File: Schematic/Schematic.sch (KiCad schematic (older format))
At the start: 28 parts, among them M1 Motor_DC, M2 Motor_DC

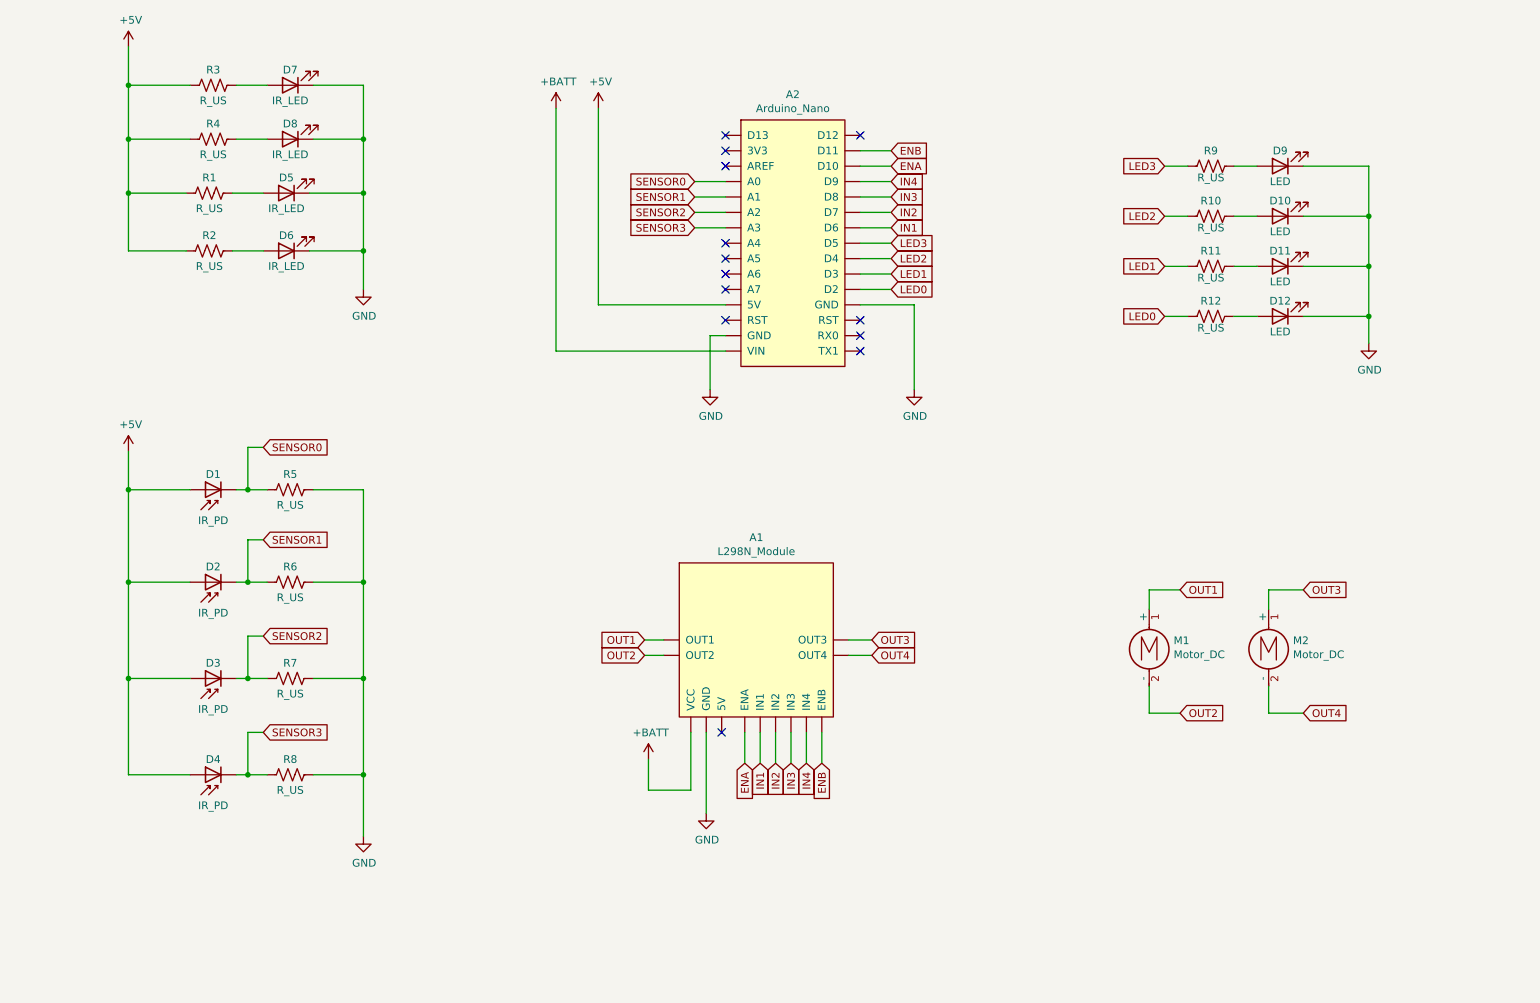
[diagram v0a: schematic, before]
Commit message: Update Schematic
- Rename Global Label
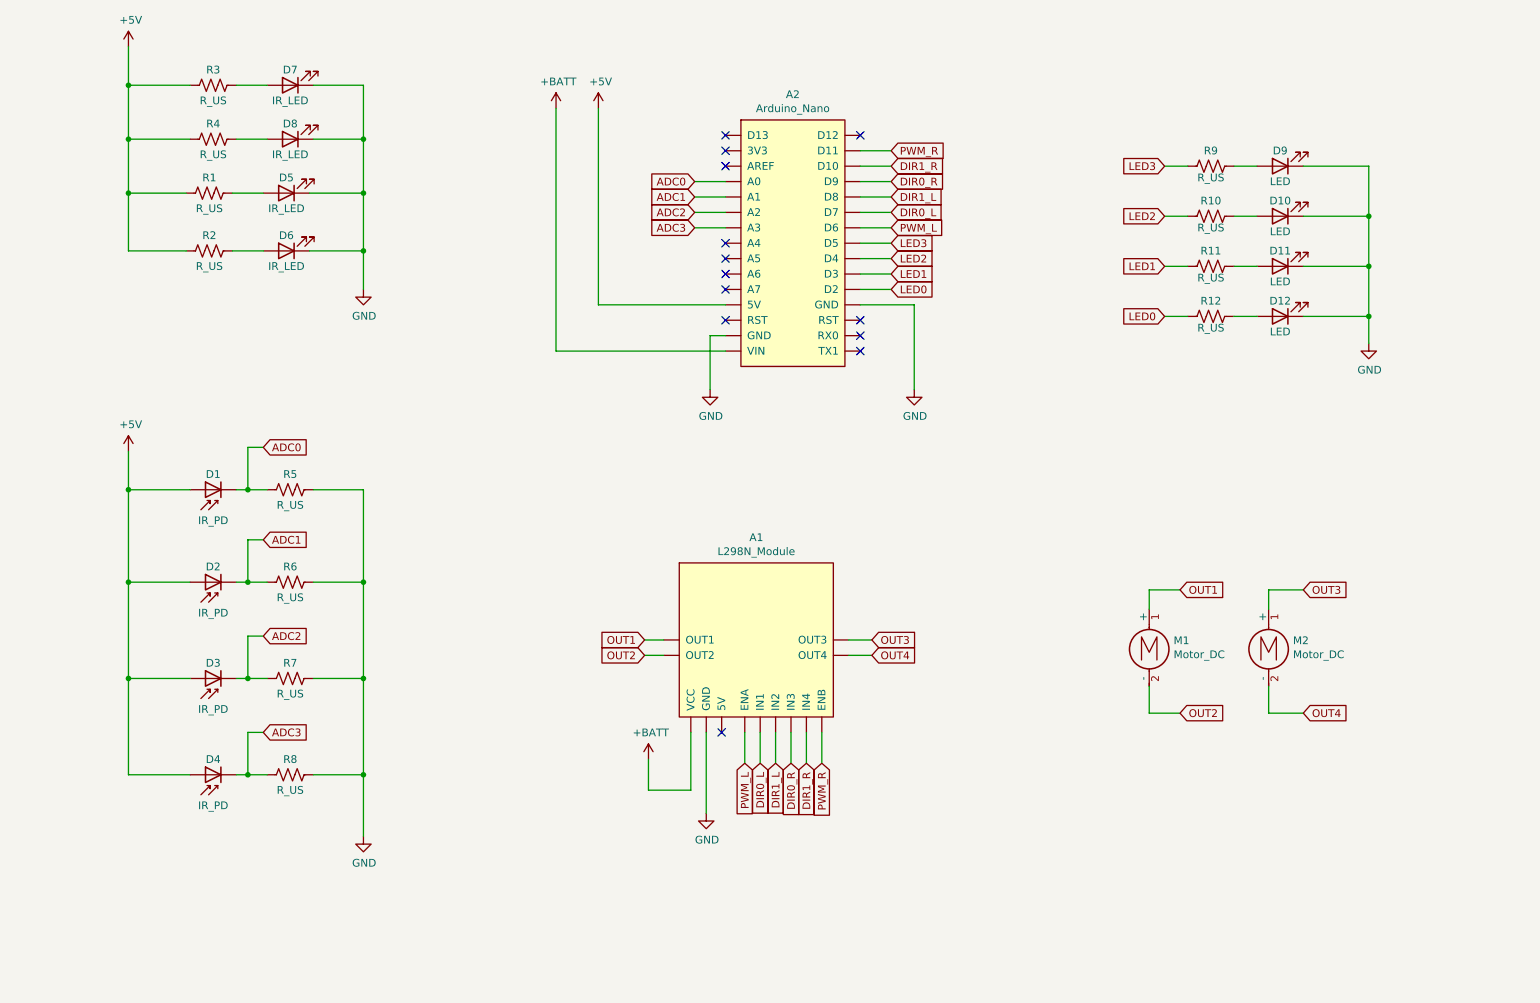
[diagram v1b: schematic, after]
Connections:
- net ENA is gone; now on net PWM_R: A1.~ (VCC), A2.~ (VIN)
- net ENB is gone; now on net PWM_R: A1.~ (VCC), A2.~ (VIN)
- net IN1 is gone; now on net PWM_R: A1.~ (VCC), A2.~ (VIN)
- net IN2 is gone; now on net PWM_R: A1.~ (VCC), A2.~ (VIN)
- net IN3 is gone; now on net PWM_R: A1.~ (VCC), A2.~ (VIN)
- net IN4 is gone; now on net PWM_R: A1.~ (VCC), A2.~ (VIN)
- net PWM_R: now reaches A2.~ (VIN)
- net SENSOR0 renamed ADC0
- net SENSOR1 renamed ADC1
- net SENSOR2 renamed ADC2
- net SENSOR3 renamed ADC3
- new net DIR0_L: A1.~ (VCC), A2.~ (VIN)
- new net DIR0_R: A1.~ (VCC), A2.~ (VIN)
- new net DIR1_L: A1.~ (VCC), A2.~ (VIN)
- new net DIR1_R: A1.~ (VCC), A2.~ (VIN)
- new net PWM_L: A1.~ (VCC), A2.~ (VIN)
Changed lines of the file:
@@
 $EndComp
 Text GLabel 5850 5775 3    50   Input ~ 0
-IN2
+DIR1_L
 Wire Wire Line
 	5850 5575 5850 5775
 Text GLabel 5750 5775 3    50   Input ~ 0
-IN1
+DIR0_L
 Wire Wire Line
 	5750 5575 5750 5775
 Text GLabel 5950 5775 3    50   Input ~ 0
-IN3
+DIR0_R
 Wire Wire Line
 	5950 5575 5950 5775
 Text GLabel 6050 5775 3    50   Input ~ 0
-IN4
+DIR1_R
 Wire Wire Line
 	6050 5575 6050 5775
-Text GLabel 6600 2200 2    50   Input ~ 0
-IN2
 Wire Wire Line
 	6400 2200 6600 2200
-Text GLabel 6600 2300 2    50   Input ~ 0
-IN1
 Wire Wire Line
 	6400 2300 6600 2300
-Text GLabel 6600 2100 2    50   Input ~ 0
-IN3
 Wire Wire Line
 	6400 2100 6600 2100
-Text GLabel 6600 2000 2    50   Input ~ 0
-IN4
 Wire Wire Line
 	6400 2000 6600 2000
-Text GLabel 5650 5775 3    50   Input ~ 0
-ENA
 Wire Wire Line
 	5650 5575 5650 5775
-Text GLabel 6150 5775 3    50   Input ~ 0
-ENB
 Wire Wire Line
 	6150 5575 6150 5775
-Text GLabel 6600 1900 2    50   Input ~ 0
-ENA
 Wire Wire Line
 	6400 1900 6600 1900
-Text GLabel 6600 1800 2    50   Input ~ 0
-ENB
 Wire Wire Line
 	6400 1800 6600 1800
@@
 	2850 4000 3175 4000
 Text GLabel 2525 3725 2    50   Input ~ 0
-SENSOR0
+ADC0
 Wire Wire Line
 	2525 3725 2425 3725
@@
 	2850 4600 3175 4600
 Text GLabel 2525 4325 2    50   Input ~ 0
-SENSOR1
+ADC1
 Wire Wire Line
 	2525 4325 2425 4325
@@
 	2850 5850 3175 5850
 Text GLabel 2525 5575 2    50   Input ~ 0
-SENSOR3
+ADC3
 Wire Wire Line
 	2525 5575 2425 5575
@@
 	2525 4950 2425 4950
 Text GLabel 2525 4950 2    50   Input ~ 0
-SENSOR2
+ADC2
 $Comp
 L power:GND #PWR04
@@
 $EndComp
 Text GLabel 5325 2000 0    50   Input ~ 0
-SENSOR0
+ADC0
 Wire Wire Line
 	5325 2000 5525 2000
 Text GLabel 5325 2100 0    50   Input ~ 0
-SENSOR1
+ADC1
 Wire Wire Line
 	5325 2100 5525 2100
 Text GLabel 5325 2200 0    50   Input ~ 0
-SENSOR2
+ADC2
 Wire Wire Line
 	5325 2200 5525 2200
 Text GLabel 5325 2300 0    50   Input ~ 0
-SENSOR3
+ADC3
 Wire Wire Line
 	5325 2300 5525 2300
@@
 NoConn ~ 5525 2700
 NoConn ~ 5525 2900
+Text GLabel 5650 5775 3    50   Input ~ 0
+PWM_L
+Text GLabel 6150 5775 3    50   Input ~ 0
+PWM_R
+Text GLabel 6600 2100 2    50   Input ~ 0
+DIR1_L
+Text GLabel 6600 2200 2    50   Input ~ 0
+DIR0_L
+Text GLabel 6600 2000 2    50   Input ~ 0
+DIR0_R
+Text GLabel 6600 1900 2    50   Input ~ 0
+DIR1_R
+Text GLabel 6600 2300 2    50   Input ~ 0
+PWM_L
+Text GLabel 6600 1800 2    50   Input ~ 0
+PWM_R
 $EndSCHEMATC

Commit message: Update Schematic
- Add resistor values
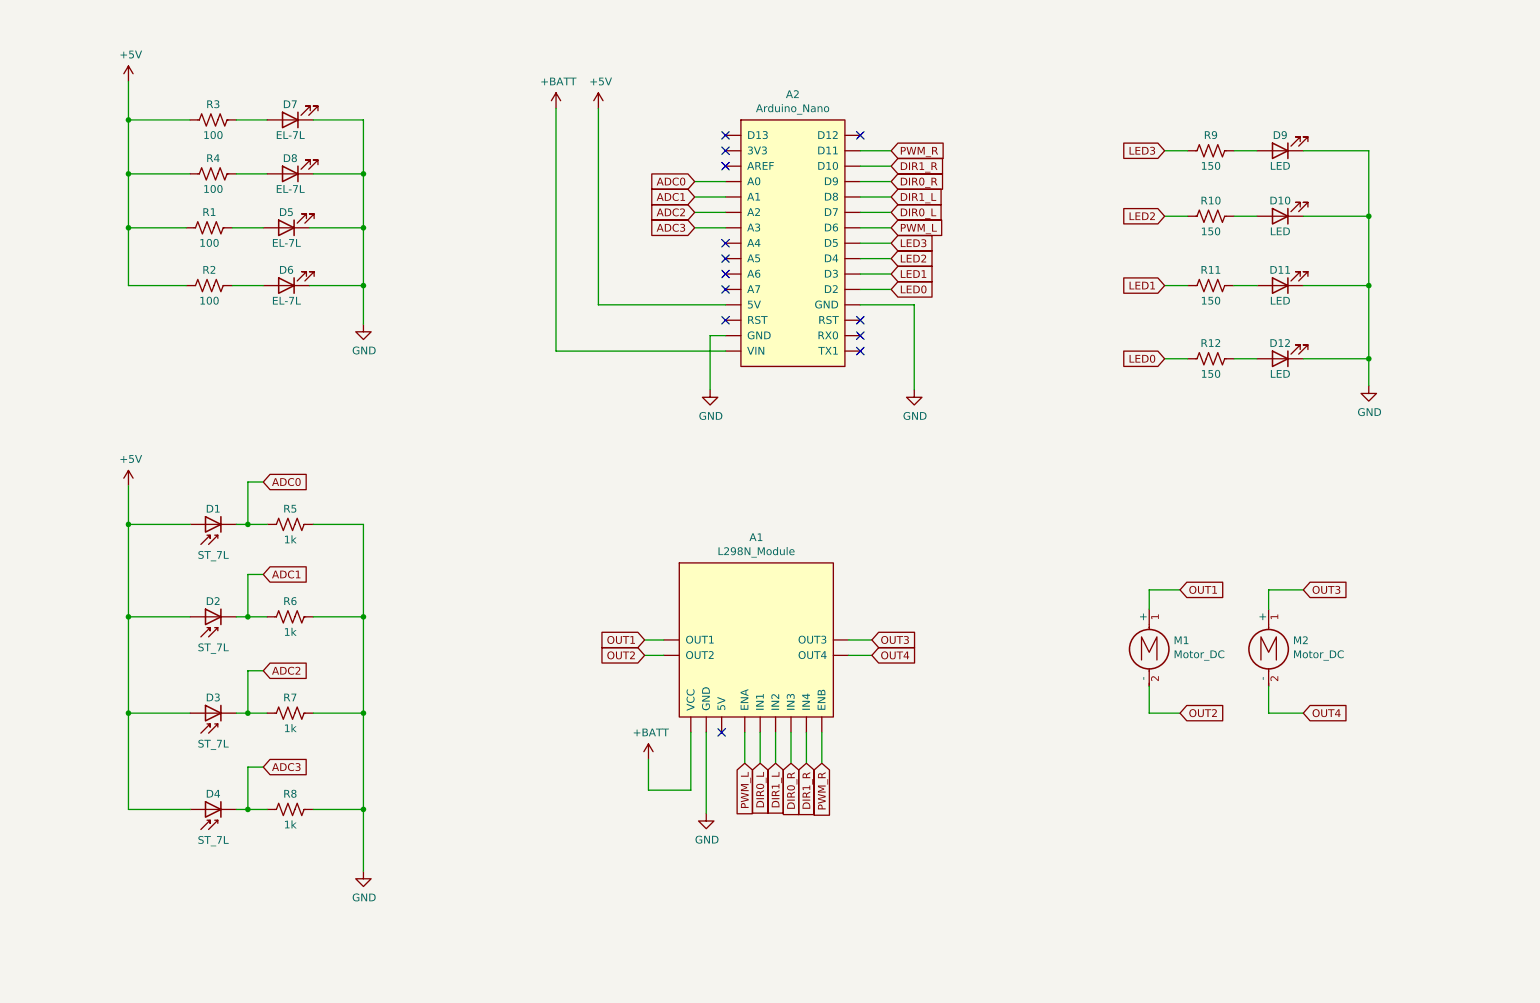
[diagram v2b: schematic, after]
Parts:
- D1, D2, D3, D4: value IR_PD -> ST_7L
- D5, D6, D7, D8: value IR_LED -> EL-7L
- R1, R2, R3, R4: value R_US -> 100
- R10, R11, R12, R9: value R_US -> 150
- R5, R6, R7, R8: value R_US -> 1k
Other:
- moved on the sheet: D1, D11, D12, D2, D3, D4, D5, D6, D7, D8, D9, R1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

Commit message: Update Schematic
- 전원부 회로 추가
- LED 저항 330옴으로 변경
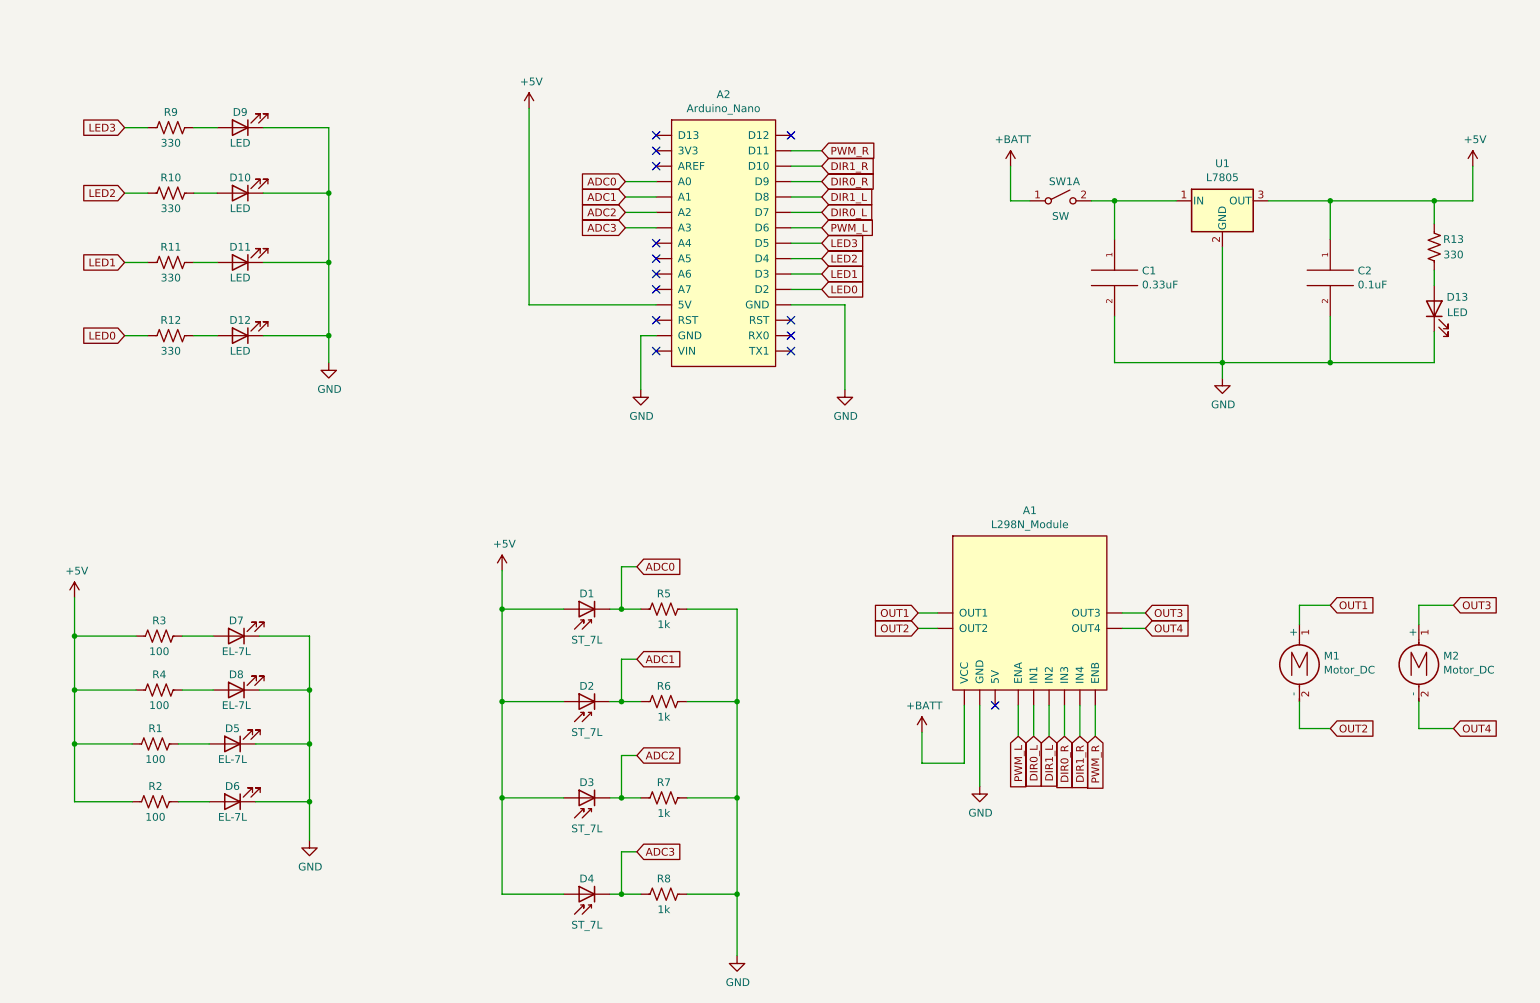
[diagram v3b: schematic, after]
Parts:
- added C1: 0.33uF, symbol pspice:C
- added C2: 0.1uF, symbol pspice:C
- added D13: LED, symbol Device:LED
- added R13: 330, symbol Device:R_US
- added SW1: SW, symbol Switch:SW_DPST_x2
- added U1: L7805, symbol Regulator_Linear:L7805
- R10, R11, R12, R9: value 150 -> 330
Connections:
- net +5V: now also C2.1, R13.2, U1.3 (OUT)
- net +BATT: now also SW1.1 (A); no longer A2.~ (VIN)
- net GND: now also C1.2, C2.2, D13.1 (K), U1.2 (GND)
- new net: C1.1, SW1.2 (B), U1.1 (IN)
- new net: D13.2 (A), R13.1
- no-connect marks 13 -> 14
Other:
- moved on the sheet: A1, A2, D1, D10, D11, D12, D2, D3, D4, D5, D6, D7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

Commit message: Update Schematic
- 스위치 위치 수정
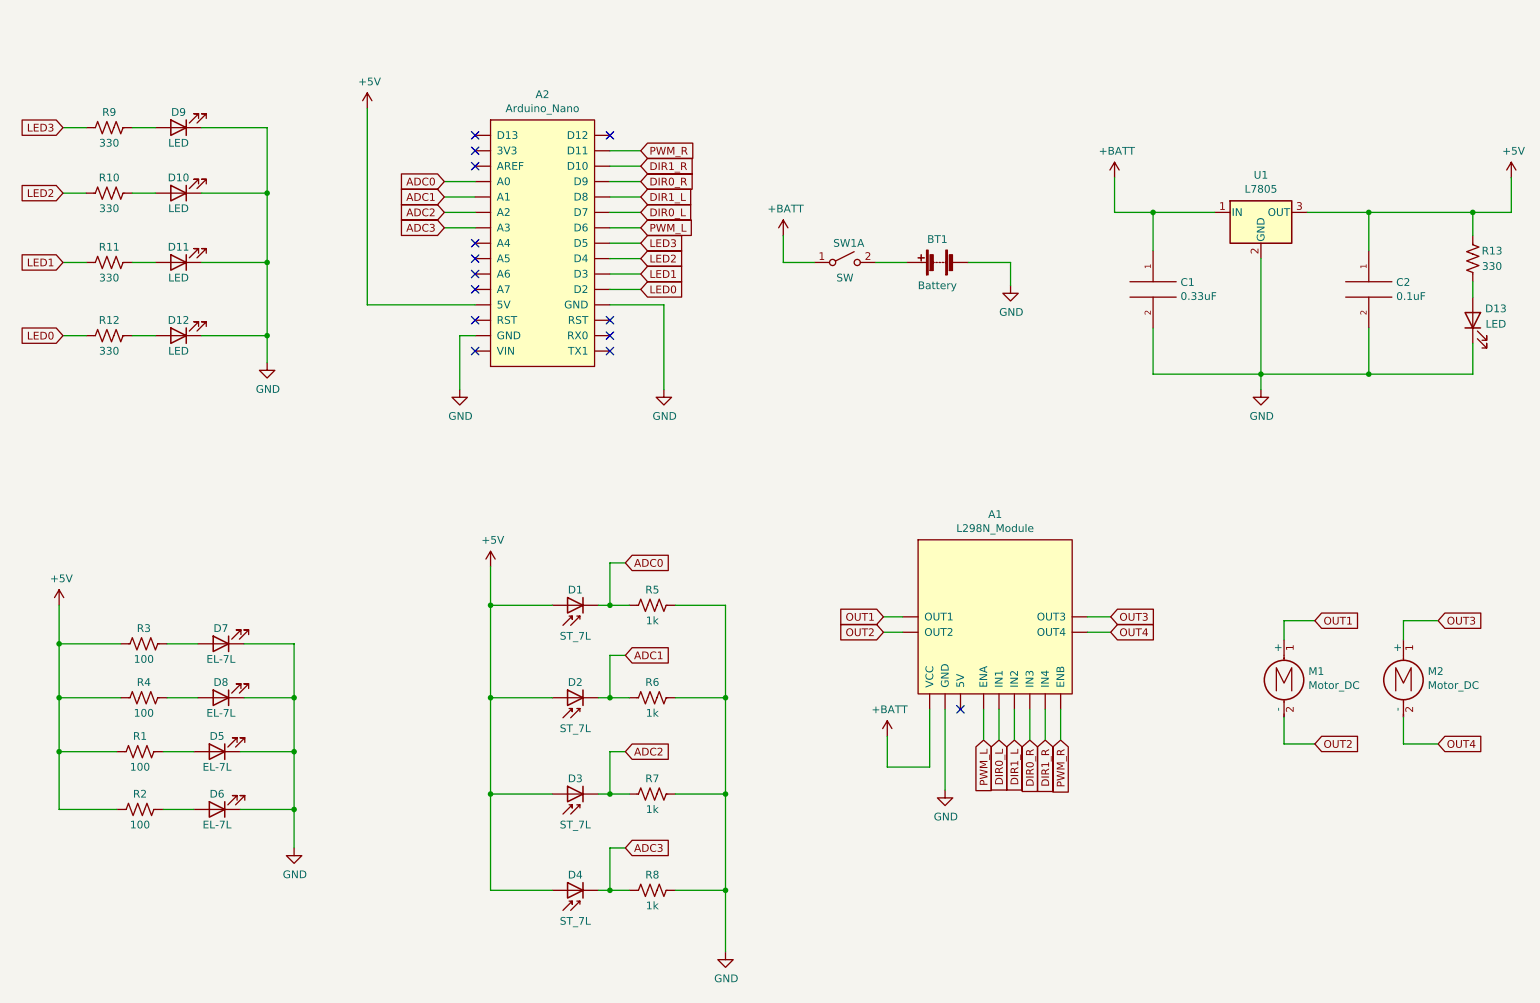
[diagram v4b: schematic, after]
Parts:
- added BT1: Battery, symbol Device:Battery
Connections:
- net +BATT: now also C1.1, U1.1 (IN)
- net GND: now also BT1.2 (-)
- new net: BT1.1 (+), SW1.2 (B)
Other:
- moved on the sheet: A1, A2, C1, C2, D1, D10, D11, D12, D13, D2, D3, D4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
